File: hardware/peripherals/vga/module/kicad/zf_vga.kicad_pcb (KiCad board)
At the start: 2 copper layers, 143 x 85 mm, 62 parts, among them J2 Z-FIGHTER Expansion Port, J3 DB15_Female, J4 DB9_Male, J5 DB9_Male, Q1 BC547, SW1 SW_DIP_x03, U1 4040, U10 74HC165, U11 AS6C6264, U12 74HC541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

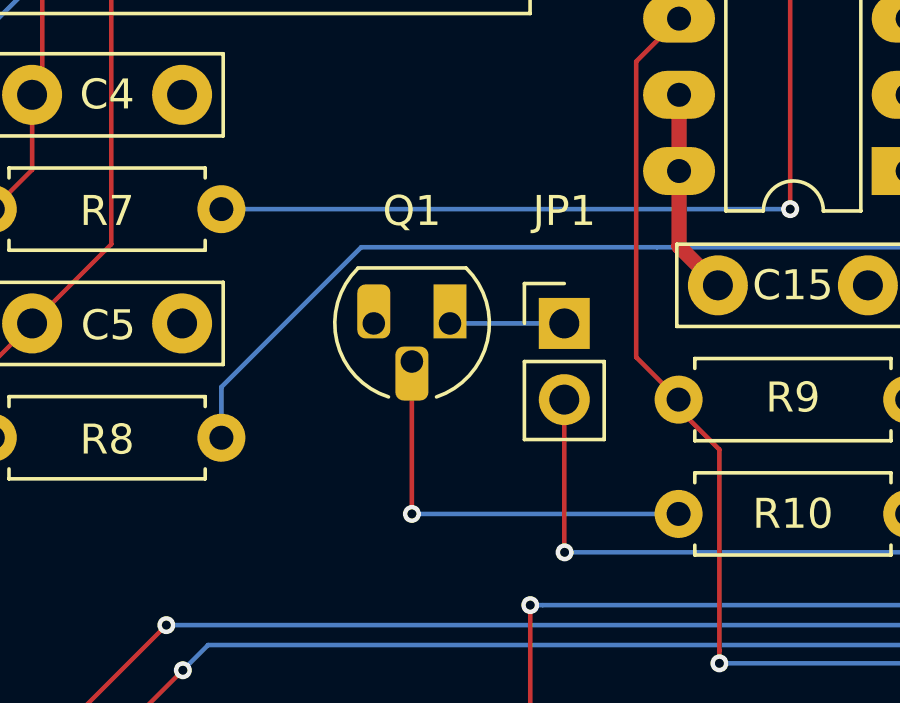
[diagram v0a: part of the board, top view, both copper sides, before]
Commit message: Changed Q1 footprint
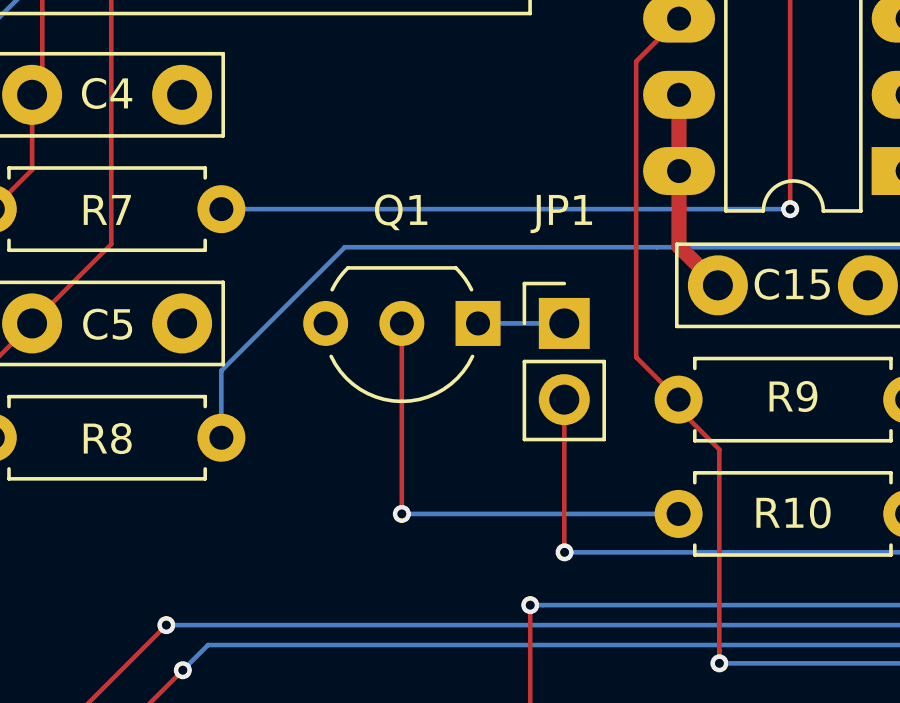
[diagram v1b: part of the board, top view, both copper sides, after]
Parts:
- C1, C2, C3: value C_Small -> 470pF
- Q1: footprint Package_TO_SOT_THT:TO-92_HandSolder -> Package_TO_SOT_THT:TO-92_Inline_Wide
- moved Q1 0.93 mm to (126.7, 50.8)
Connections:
- U11 pad 28: (no net) -> VCC
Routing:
- net VCC: track 74.5 -> 86.5 mm
- net (no net): track 12.0 -> 0.00 mm
- net Net-(Q1-Pad2): track 13.9 -> 15.6 mm
- net Net-(JP1-Pad1): track 3.81 -> 2.88 mm
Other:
- board text added: "Z-FIGHTER VGA Module Rev. 2a @tangent3D 2022"
- board text removed: "Z-FIGHTER VGA Module Rev. 2 @tangent3D 2022"

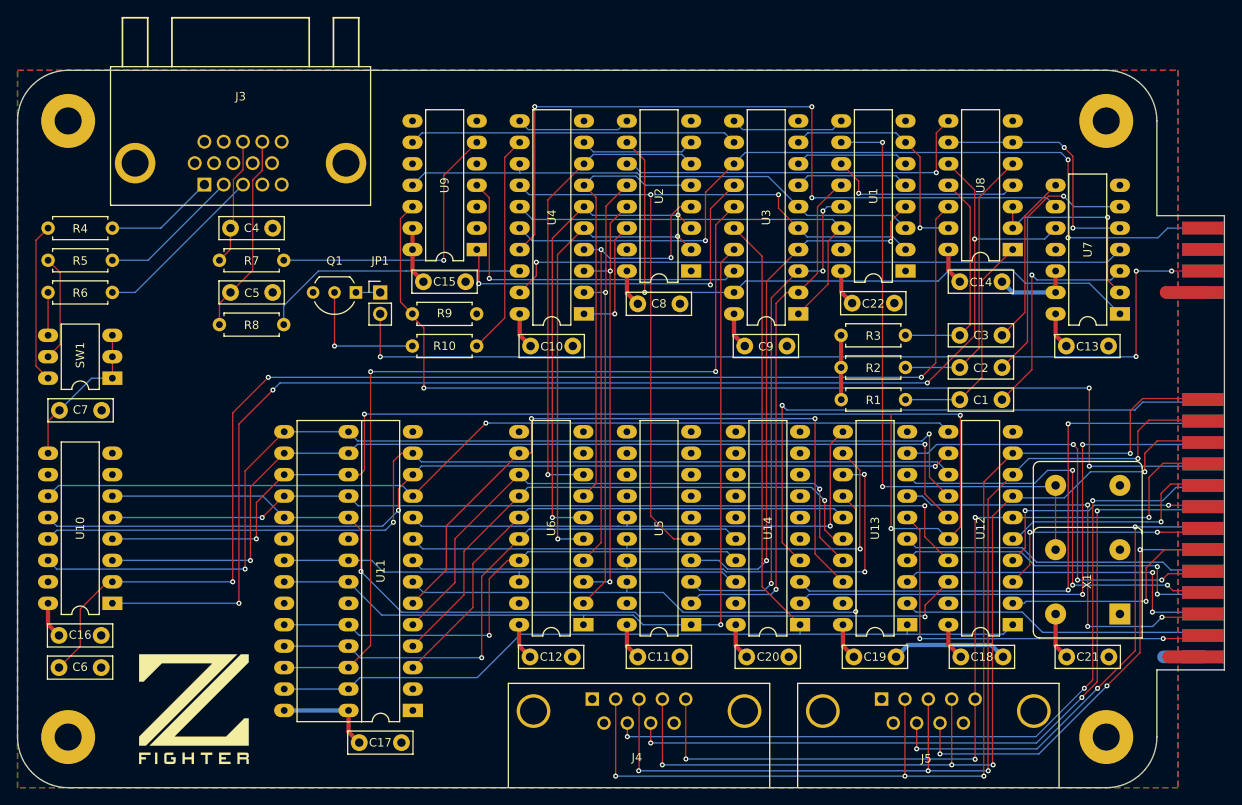
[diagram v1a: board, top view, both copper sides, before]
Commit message: Fixed interrupt circuit, routing improvements
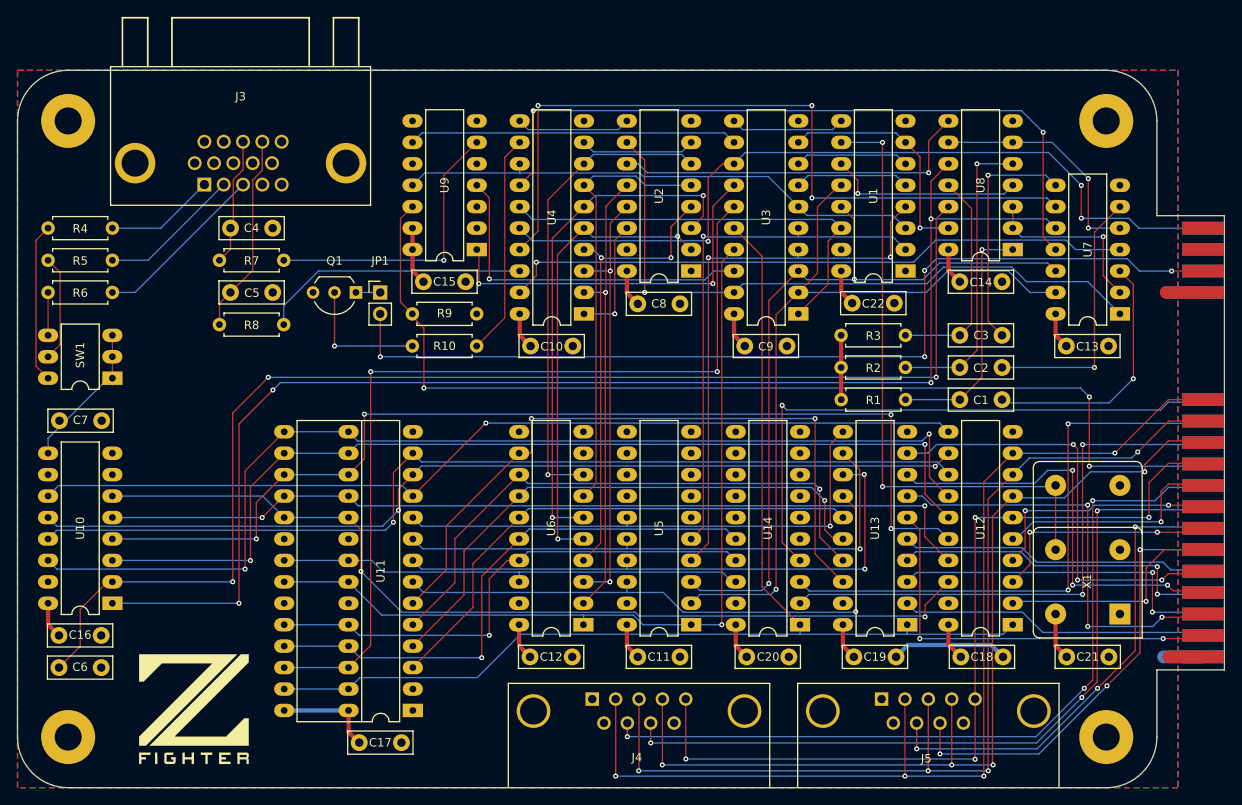
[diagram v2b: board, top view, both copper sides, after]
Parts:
- moved C7 1.23 mm to (96.6, 66.0)
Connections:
- U11 pad 28: VCC -> (no net)
- U4 pad 14: P5 -> P8.P7
- U7 pad 11: Net-(U7-Pad11) -> P8.P7
- U7 pad 12: GND -> P7
- U7 pad 13: GND -> P8
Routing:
- net P8.P7: track 0.00 -> 85.4 mm, vias 0 -> 2
- net P5: track 93.8 -> 62.1 mm, vias 2 -> 1
- net P8: track 62.8 -> 94.3 mm
- net P7: track 61.2 -> 89.9 mm, vias 3 -> 2
- net D5: track 149.3 -> 125.1 mm
- net VCC: track 86.5 -> 74.5 mm
- net (no net): track 0.00 -> 12.0 mm
- net GND: track 40.4 -> 31.0 mm
- net Net-(C3-Pad1): track 20.4 -> 28.1 mm, vias 0 -> 1
- net L4: track 55.9 -> 61.2 mm
- net #RESET: track 99.5 -> 96.1 mm
- net PA0: track 130.6 -> 127.5 mm
- net Net-(C1-Pad1): track 27.3 -> 30.3 mm
- net #LDPULSE: track 159.5 -> 162.3 mm
- net #PRPULSE: track 23.8 -> 21.1 mm
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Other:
- board text added: "Z-FIGHTER VGA Module Rev. 2b @tangent3D 2022"
- board text removed: "Z-FIGHTER VGA Module Rev. 2a @tangent3D 2022"

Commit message: Routing tweaks
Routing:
- net #HSYNC: track 35.2 -> 40.8 mm
- net L4: track 61.2 -> 66.7 mm, vias 2 -> 3
- net L2: track 56.4 -> 61.8 mm, vias 1 -> 2
- net DATARDY: track 124.1 -> 127.4 mm
- net L5: track 55.0 -> 57.5 mm, vias 2 -> 3
- net A4: track 82.8 -> 82.0 mm
- net P6: track 66.2 -> 67.0 mm
- net D6: track 105.5 -> 104.9 mm

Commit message: Routing
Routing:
- net A9: track 62.5 -> 61.7 mm
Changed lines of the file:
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@@
     (thickness 1.6)
     (drawings 16)
-    (tracks 992)
+    (tracks 991)
     (zones 0)
     (modules 62)
@@
   (segment (start 150.064963 80.023996) (end 150.064959 80.024) (width 0.1524) (layer B.Cu) (net 60))
   (segment (start 153.67 80.023996) (end 150.064963 80.023996) (width 0.1524) (layer B.Cu) (net 60))
-  (segment (start 172.54761 49.78539) (end 171.519 50.814) (width 0.1524) (layer B.Cu) (net 61))
-  (segment (start 194.36017 49.78539) (end 172.54761 49.78539) (width 0.1524) (layer B.Cu) (net 61))
-  (segment (start 196.33212 47.81344) (end 194.36017 49.78539) (width 0.1524) (layer B.Cu) (net 61))
-  (segment (start 204.43472 47.81344) (end 196.33212 47.81344) (width 0.1524) (layer B.Cu) (net 61))
-  (segment (start 213.42056 49.53556) (end 206.15684 49.53556) (width 0.1524) (layer B.Cu) (net 61))
-  (segment (start 206.15684 49.53556) (end 204.43472 47.81344) (width 0.1524) (layer B.Cu) (net 61))
-  (segment (start 217.239 53.354) (end 213.42056 49.53556) (width 0.1524) (layer B.Cu) (net 61))
   (via (at 160.74672 50.814) (size 0.6) (drill 0.3) (layers F.Cu B.Cu) (net 61))
   (segment (start 171.519 50.814) (end 160.74672 50.814) (width 0.1524) (layer B.Cu) (net 61))
   (segment (start 160.74672 34.96172) (end 160.74672 50.814) (width 0.1524) (layer F.Cu) (net 61))
   (segment (start 158.819 33.034) (end 160.74672 34.96172) (width 0.1524) (layer F.Cu) (net 61))
+  (segment (start 172.54761 49.78539) (end 171.519 50.814) (width 0.1524) (layer B.Cu) (net 61))
+  (segment (start 194.34417 49.78539) (end 172.54761 49.78539) (width 0.1524) (layer B.Cu) (net 61))
+  (segment (start 196.31612 47.81344) (end 194.34417 49.78539) (width 0.1524) (layer B.Cu) (net 61))
+  (segment (start 206.20784 49.53556) (end 204.48572 47.81344) (width 0.1524) (layer B.Cu) (net 61))
+  (segment (start 204.48572 47.81344) (end 196.31612 47.81344) (width 0.1524) (layer B.Cu) (net 61))
+  (segment (start 213.42056 49.53556) (end 206.20784 49.53556) (width 0.1524) (layer B.Cu) (net 61))
+  (segment (start 217.239 53.354) (end 213.42056 49.53556) (width 0.1524) (layer B.Cu) (net 61))
   (via (at 149.416349 77.483998) (size 0.6) (drill 0.3) (layers F.Cu B.Cu) (net 62))
   (via (at 167.87904 39.51272) (size 0.6) (drill 0.3) (layers F.Cu B.Cu) (net 62))
@@
   (segment (start 153.688999 89.064) (end 153.688999 90.165001) (width 0.1524) (layer B.Cu) (net 73))
   (segment (start 125.839 85.104) (end 118.219 85.104) (width 0.1524) (layer B.Cu) (net 73))
-  (segment (start 129.779 89.044) (end 125.839 85.104) (width 0.1524) (layer B.Cu) (net 73))
-  (segment (start 159.588999 89.044) (end 129.779 89.044) (width 0.1524) (layer B.Cu) (net 73))
-  (segment (start 160.728999 90.184) (end 159.588999 89.044) (width 0.1524) (layer B.Cu) (net 73))
-  (segment (start 166.439 90.184) (end 160.728999 90.184) (width 0.1524) (layer B.Cu) (net 73))
   (via (at 170.066558 90.184) (size 0.6) (drill 0.3) (layers F.Cu B.Cu) (net 73))
   (segment (start 166.439 90.184) (end 170.066558 90.184) (width 0.1524) (layer B.Cu) (net 73))
   (segment (start 170.066558 47.186442) (end 170.066558 90.184) (width 0.1524) (layer F.Cu) (net 73))
   (segment (start 171.519 45.734) (end 170.066558 47.186442) (width 0.1524) (layer F.Cu) (net 73))
+  (segment (start 166.439 90.184) (end 160.728999 90.184) (width 0.1524) (layer B.Cu) (net 73))
+  (segment (start 160.728999 90.184) (end 159.588999 89.044) (width 0.1524) (layer B.Cu) (net 73))
+  (segment (start 159.588999 89.044) (end 129.779 89.044) (width 0.1524) (layer B.Cu) (net 73))
+  (segment (start 129.779 89.044) (end 125.839 85.104) (width 0.1524) (layer B.Cu) (net 73))
   (segment (start 118.219 97.804) (end 125.839 97.804) (width 0.1524) (layer B.Cu) (net 74))
   (segment (start 127.189 96.454) (end 125.839 97.804) (width 0.1524) (layer B.Cu) (net 74))
@@
   (segment (start 158.819 86.353999) (end 158.818999 86.354) (width 0.1524) (layer B.Cu) (net 84))
   (segment (start 158.819 85.104) (end 158.819 86.353999) (width 0.1524) (layer B.Cu) (net 84))
-  (segment (start 185.86039 88.704) (end 185.939 88.62539) (width 0.1524) (layer B.Cu) (net 84))
-  (segment (start 165.479 88.704) (end 185.86039 88.704) (width 0.1524) (layer B.Cu) (net 84))
-  (segment (start 163.139 86.364) (end 165.479 88.704) (width 0.1524) (layer B.Cu) (net 84))
-  (segment (start 134.719 86.364) (end 163.139 86.364) (width 0.1524) (layer B.Cu) (net 84))
-  (segment (start 133.459 85.104) (end 134.719 86.364) (width 0.1524) (layer B.Cu) (net 84))
   (via (at 185.939 88.62539) (size 0.6) (drill 0.3) (layers F.Cu B.Cu) (net 84))
   (segment (start 185.939 88.201126) (end 185.939 88.62539) (width 0.1524) (layer F.Cu) (net 84))
   (segment (start 185.939 76.464) (end 185.939 88.201126) (width 0.1524) (layer F.Cu) (net 84))
   (segment (start 184.419 74.944) (end 185.939 76.464) (width 0.1524) (layer F.Cu) (net 84))
+  (segment (start 133.459 85.104) (end 134.719 86.364) (width 0.1524) (layer B.Cu) (net 84))
+  (segment (start 134.719 86.364) (end 163.139 86.364) (width 0.1524) (layer B.Cu) (net 84))
+  (segment (start 163.139 86.364) (end 165.479 88.704) (width 0.1524) (layer B.Cu) (net 84))
+  (segment (start 165.479 88.704) (end 185.86039 88.704) (width 0.1524) (layer B.Cu) (net 84))
+  (segment (start 185.86039 88.704) (end 185.939 88.62539) (width 0.1524) (layer B.Cu) (net 84))
   (segment (start 158.83039 83.59261) (end 158.83039 82.564) (width 0.1524) (layer B.Cu) (net 85))
   (segment (start 184.369 72.354) (end 184.419 72.404) (width 0.1524) (layer B.Cu) (net 85))
@@
   (segment (start 118.219 90.184) (end 125.839 90.184) (width 0.1524) (layer B.Cu) (net 90))
   (via (at 142.514 91.444) (size 0.6) (drill 0.3) (layers F.Cu B.Cu) (net 90))
-  (segment (start 146.05 82.564) (end 144.6976 82.564) (width 0.1524) (layer F.Cu) (net 90))
-  (segment (start 144.6976 82.564) (end 142.514 84.7476) (width 0.1524) (layer F.Cu) (net 90))
-  (segment (start 142.514 84.7476) (end 142.514 91.444) (width 0.1524) (layer F.Cu) (net 90))
   (segment (start 127.099 91.444) (end 142.514 91.444) (width 0.1524) (layer B.Cu) (net 90))
   (segment (start 125.839 90.184) (end 127.099 91.444) (width 0.1524) (layer B.Cu) (net 90))
@@
   (segment (start 147.107609 81.53539) (end 170.69039 81.53539) (width 0.1524) (layer B.Cu) (net 90))
   (segment (start 170.69039 81.53539) (end 171.719 82.564) (width 0.1524) (layer B.Cu) (net 90))
+  (segment (start 142.514 86.1) (end 142.514 91.444) (width 0.1524) (layer F.Cu) (net 90))
+  (segment (start 146.05 82.564) (end 142.514 86.1) (width 0.1524) (layer F.Cu) (net 90))
   (segment (start 146.05 80.024) (end 141.619 84.455) (width 0.1524) (layer F.Cu) (net 91))
   (segment (start 141.619 84.455) (end 141.619 94.094) (width 0.1524) (layer F.Cu) (net 91))
@@
   (via (at 194.15 89.25) (size 0.6) (drill 0.3) (layers F.Cu B.Cu) (net 104))
   (via (at 127.314 83.874) (size 0.6) (drill 0.3) (layers F.Cu B.Cu) (net 104))
-  (segment (start 194.15 89.25) (end 194.054 89.154) (width 0.1524) (layer B.Cu) (net 104))
-  (segment (start 194.054 89.154) (end 160.248999 89.154) (width 0.1524) (layer B.Cu) (net 104))
-  (segment (start 160.248999 89.154) (end 159.798999 88.704) (width 0.1524) (layer B.Cu) (net 104))
-  (segment (start 159.798999 88.704) (end 132.144 88.704) (width 0.1524) (layer B.Cu) (net 104))
-  (segment (start 132.144 88.704) (end 127.314 83.874) (width 0.1524) (layer B.Cu) (net 104))
   (segment (start 127.314 78.959) (end 127.314 83.874) (width 0.1524) (layer F.Cu) (net 104))
   (segment (start 125.839 77.484) (end 127.314 78.959) (width 0.1524) (layer F.Cu) (net 104))
@@
   (segment (start 196.61248 85.104) (end 194.15 87.56648) (width 0.1524) (layer F.Cu) (net 104))
   (segment (start 196.919 85.104) (end 196.61248 85.104) (width 0.1524) (layer F.Cu) (net 104))
+  (segment (start 194.15 89.25) (end 194.054 89.154) (width 0.1524) (layer B.Cu) (net 104))
+  (segment (start 194.054 89.154) (end 160.248999 89.154) (width 0.1524) (layer B.Cu) (net 104))
+  (segment (start 160.248999 89.154) (end 159.798999 88.704) (width 0.1524) (layer B.Cu) (net 104))
+  (segment (start 159.798999 88.704) (end 132.144 88.704) (width 0.1524) (layer B.Cu) (net 104))
+  (segment (start 132.144 88.704) (end 127.314 83.874) (width 0.1524) (layer B.Cu) (net 104))
   (segment (start 196.919 72.194001) (end 196.919 72.404) (width 0.1524) (layer B.Cu) (net 105))
   (segment (start 195.617609 70.89261) (end 196.919 72.194001) (width 0.1524) (layer B.Cu) (net 105))

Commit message: Schematic media, fixes
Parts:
- R1, R2: value 220 -> 220Ω
- R10: value 1K -> 1KΩ
- R3: value 200 -> 220Ω
